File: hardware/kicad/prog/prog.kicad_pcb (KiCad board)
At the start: 2 copper layers, 174 x 134 mm, 1 part, among them J1 AES_PROG

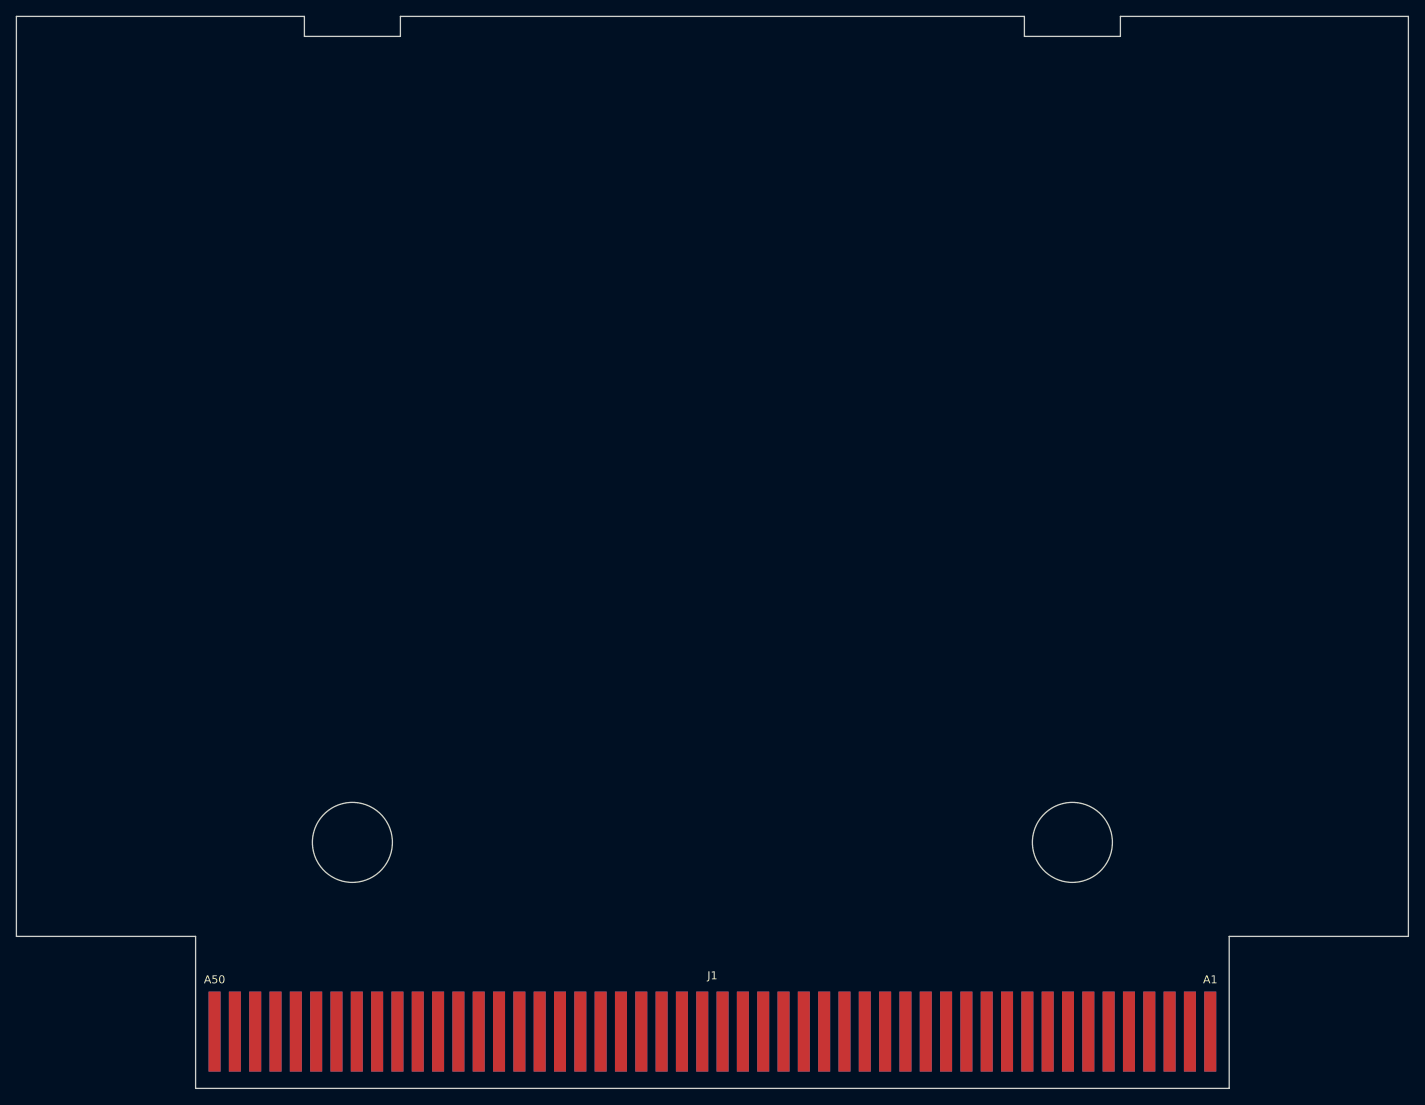
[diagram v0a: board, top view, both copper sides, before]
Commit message: Circuits imprimés 2 couches : placement et affectation des broches FPGA
- hardware/gen/pcb.py : empreintes et réseaux depuis boards.py, contour
  depuis outline.py ; ancres placées (contacts, rangée de tampons, FPGA,
  mémoires ; CHA : Pico au centre, microSD et bouton en haut), passifs
  au plus près de leur broche, masse coulée sur les deux faces.
- --pins : signaux des FPGA affectés aux broches tournées vers leur
  cible en conservant l'ordre circulaire (pins_opt.json, repris par
  fpga_pins.py) ; stable en trois passes.
- boards.py : canaux des tampons triés selon la position des contacts.
- hardware/gen/route.py : export Specctra, Freerouting, relecture de la
  session, DRC.
Placement-routage FPGA avec les nouvelles broches : en cours de
vérification.

Co-Authored-By: Claude Opus 5.5 <noreply@anthropic.com>
Claude-Session: https://claude.ai/code/session_01WKfXP1YJ8otGxZ5dsY6Agh
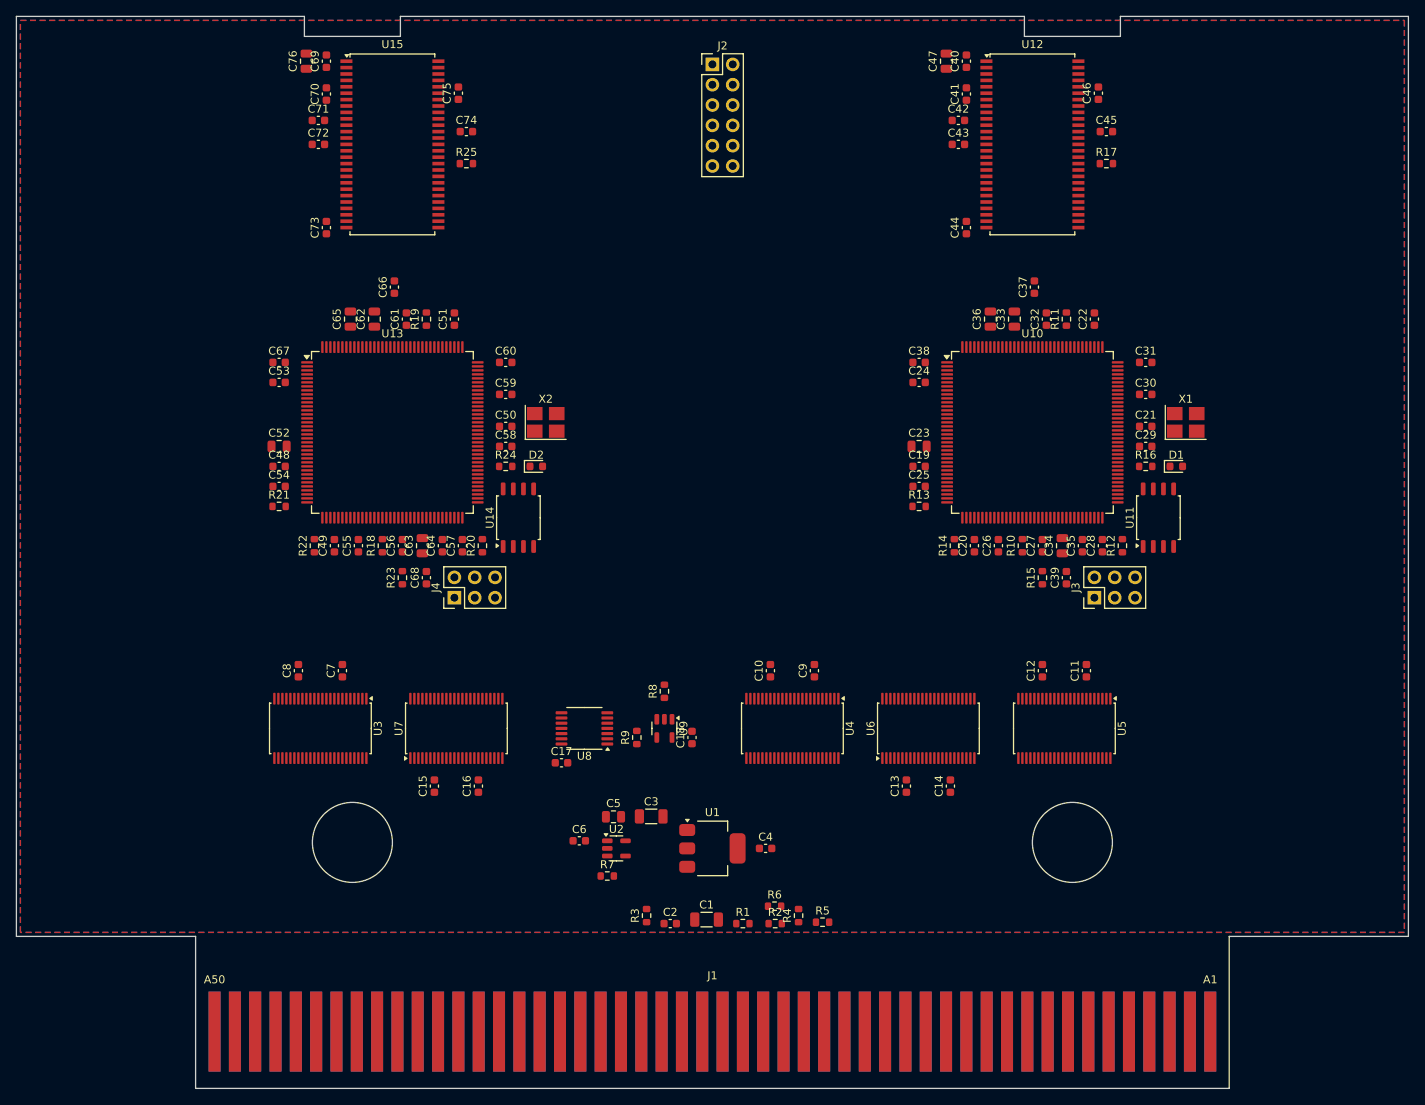
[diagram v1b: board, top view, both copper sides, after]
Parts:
- added C1: 22u, Capacitor_SMD:C_1206_3216Metric, F.Cu at (149.3, 158.9)
- added C10: 100n, Capacitor_SMD:C_0603_1608Metric, F.Cu at (157.2, 127.8)
- added C11: 100n, Capacitor_SMD:C_0603_1608Metric, F.Cu at (196.8, 127.8)
- added C12: 100n, Capacitor_SMD:C_0603_1608Metric, F.Cu at (191.2, 127.8)
- added C13: 100n, Capacitor_SMD:C_0603_1608Metric, F.Cu at (174.2, 142.2)
- added C14: 100n, Capacitor_SMD:C_0603_1608Metric, F.Cu at (179.8, 142.2)
- added C15: 100n, Capacitor_SMD:C_0603_1608Metric, F.Cu at (115.2, 142.2)
- added C16: 100n, Capacitor_SMD:C_0603_1608Metric, F.Cu at (120.8, 142.2)
- added C17: 100n, Capacitor_SMD:C_0603_1608Metric, F.Cu at (131.1, 139.3)
- added C18: 100n, Capacitor_SMD:C_0603_1608Metric, F.Cu at (147.4, 136.1)
- added C19: 100n, Capacitor_SMD:C_0603_1608Metric, F.Cu at (175.8, 102.2)
- added C2: 100n, Capacitor_SMD:C_0603_1608Metric, F.Cu at (144.7, 159.4)
- added C20: 100n, Capacitor_SMD:C_0603_1608Metric, F.Cu at (182.8, 112.2)
- added C21: 100n, Capacitor_SMD:C_0603_1608Metric, F.Cu at (204.2, 97.2)
- added C22: 100n, Capacitor_SMD:C_0603_1608Metric, F.Cu at (197.8, 83.8)
- added C23: 10u, Capacitor_SMD:C_0805_2012Metric, F.Cu at (175.8, 99.8)
- added C24: 100n, Capacitor_SMD:C_0603_1608Metric, F.Cu at (175.8, 91.8)
- added C25: 100n, Capacitor_SMD:C_0603_1608Metric, F.Cu at (175.8, 104.8)
- added C26: 100n, Capacitor_SMD:C_0603_1608Metric, F.Cu at (185.8, 112.2)
- added C27: 100n, Capacitor_SMD:C_0603_1608Metric, F.Cu at (191.2, 112.2)
- added C28: 100n, Capacitor_SMD:C_0603_1608Metric, F.Cu at (198.8, 112.2)
- added C29: 100n, Capacitor_SMD:C_0603_1608Metric, F.Cu at (204.2, 99.8)
- added C3: 22u, Capacitor_SMD:C_1206_3216Metric, F.Cu at (142.3, 146.0)
- added C30: 100n, Capacitor_SMD:C_0603_1608Metric, F.Cu at (204.2, 93.2)
- added C31: 100n, Capacitor_SMD:C_0603_1608Metric, F.Cu at (204.2, 89.2)
- added C32: 100n, Capacitor_SMD:C_0603_1608Metric, F.Cu at (191.8, 83.8)
- added C33: 10u, Capacitor_SMD:C_0805_2012Metric, F.Cu at (187.8, 83.8)
- added C34: 10u, Capacitor_SMD:C_0805_2012Metric, F.Cu at (193.8, 112.2)
- added C35: 100n, Capacitor_SMD:C_0603_1608Metric, F.Cu at (196.2, 112.2)
- added C36: 10u, Capacitor_SMD:C_0805_2012Metric, F.Cu at (184.8, 83.8)
- added C37: 100n, Capacitor_SMD:C_0603_1608Metric, F.Cu at (190.2, 79.8)
- added C38: 100n, Capacitor_SMD:C_0603_1608Metric, F.Cu at (175.8, 89.2)
- added C39: 100n, Capacitor_SMD:C_0603_1608Metric, F.Cu at (194.2, 116.2)
- added C4: 100n, Capacitor_SMD:C_0603_1608Metric, F.Cu at (156.7, 150.0)
- added C40: 100n, Capacitor_SMD:C_0603_1608Metric, F.Cu at (181.8, 51.6)
- added C41: 100n, Capacitor_SMD:C_0603_1608Metric, F.Cu at (181.8, 55.7)
- added C42: 100n, Capacitor_SMD:C_0603_1608Metric, F.Cu at (180.8, 59.0)
- added C43: 100n, Capacitor_SMD:C_0603_1608Metric, F.Cu at (180.8, 62.0)
- added C44: 100n, Capacitor_SMD:C_0603_1608Metric, F.Cu at (181.8, 72.4)
- added C45: 100n, Capacitor_SMD:C_0603_1608Metric, F.Cu at (199.2, 60.4)
- added C46: 100n, Capacitor_SMD:C_0603_1608Metric, F.Cu at (198.2, 55.6)
- added C47: 10u, Capacitor_SMD:C_0805_2012Metric, F.Cu at (179.2, 51.6)
- added C48: 100n, Capacitor_SMD:C_0603_1608Metric, F.Cu at (95.8, 102.2)
- added C49: 100n, Capacitor_SMD:C_0603_1608Metric, F.Cu at (102.8, 112.2)
- added C5: 10u, Capacitor_SMD:C_0805_2012Metric, F.Cu at (137.6, 146.1)
- added C50: 100n, Capacitor_SMD:C_0603_1608Metric, F.Cu at (124.2, 97.2)
- added C51: 100n, Capacitor_SMD:C_0603_1608Metric, F.Cu at (117.8, 83.8)
- added C52: 10u, Capacitor_SMD:C_0805_2012Metric, F.Cu at (95.8, 99.8)
- added C53: 100n, Capacitor_SMD:C_0603_1608Metric, F.Cu at (95.8, 91.8)
- added C54: 100n, Capacitor_SMD:C_0603_1608Metric, F.Cu at (95.8, 104.8)
- added C55: 100n, Capacitor_SMD:C_0603_1608Metric, F.Cu at (105.8, 112.2)
- added C56: 100n, Capacitor_SMD:C_0603_1608Metric, F.Cu at (111.2, 112.2)
- added C57: 100n, Capacitor_SMD:C_0603_1608Metric, F.Cu at (118.8, 112.2)
- added C58: 100n, Capacitor_SMD:C_0603_1608Metric, F.Cu at (124.2, 99.8)
- added C59: 100n, Capacitor_SMD:C_0603_1608Metric, F.Cu at (124.2, 93.2)
- added C6: 1u, Capacitor_SMD:C_0603_1608Metric, F.Cu at (133.4, 149.1)
- added C60: 100n, Capacitor_SMD:C_0603_1608Metric, F.Cu at (124.2, 89.2)
- added C61: 100n, Capacitor_SMD:C_0603_1608Metric, F.Cu at (111.8, 83.8)
- added C62: 10u, Capacitor_SMD:C_0805_2012Metric, F.Cu at (107.8, 83.8)
- added C63: 10u, Capacitor_SMD:C_0805_2012Metric, F.Cu at (113.8, 112.2)
- added C64: 100n, Capacitor_SMD:C_0603_1608Metric, F.Cu at (116.2, 112.2)
- added C65: 10u, Capacitor_SMD:C_0805_2012Metric, F.Cu at (104.8, 83.8)
- added C66: 100n, Capacitor_SMD:C_0603_1608Metric, F.Cu at (110.2, 79.8)
- added C67: 100n, Capacitor_SMD:C_0603_1608Metric, F.Cu at (95.8, 89.2)
- added C68: 100n, Capacitor_SMD:C_0603_1608Metric, F.Cu at (114.2, 116.2)
- added C69: 100n, Capacitor_SMD:C_0603_1608Metric, F.Cu at (101.8, 51.6)
- added C7: 100n, Capacitor_SMD:C_0603_1608Metric, F.Cu at (103.8, 127.8)
- added C70: 100n, Capacitor_SMD:C_0603_1608Metric, F.Cu at (101.8, 55.7)
- added C71: 100n, Capacitor_SMD:C_0603_1608Metric, F.Cu at (100.8, 59.0)
- added C72: 100n, Capacitor_SMD:C_0603_1608Metric, F.Cu at (100.8, 62.0)
- added C73: 100n, Capacitor_SMD:C_0603_1608Metric, F.Cu at (101.8, 72.4)
- added C74: 100n, Capacitor_SMD:C_0603_1608Metric, F.Cu at (119.2, 60.4)
- added C75: 100n, Capacitor_SMD:C_0603_1608Metric, F.Cu at (118.2, 55.6)
- added C76: 10u, Capacitor_SMD:C_0805_2012Metric, F.Cu at (99.2, 51.6)
- added C8: 100n, Capacitor_SMD:C_0603_1608Metric, F.Cu at (98.2, 127.8)
- added C9: 100n, Capacitor_SMD:C_0603_1608Metric, F.Cu at (162.8, 127.8)
- added D1: LED, LED_SMD:LED_0603_1608Metric, F.Cu at (208.0, 102.2)
- added D2: LED, LED_SMD:LED_0603_1608Metric, F.Cu at (128.0, 102.2)
- added J2: Câble PROG-CHA, Connector_PinHeader_2.54mm:PinHeader_2x06_P2.54mm_Vertical, F.Cu at (150.0, 52.0)
- added J3: PROG P, Connector_PinHeader_2.54mm:PinHeader_2x03_P2.54mm_Vertical, F.Cu at (197.8, 118.7)
- added J4: PROG V, Connector_PinHeader_2.54mm:PinHeader_2x03_P2.54mm_Vertical, F.Cu at (117.8, 118.7)
- added R1: 0, Resistor_SMD:R_0603_1608Metric, F.Cu at (153.8, 159.4)
- added R10: 100, Resistor_SMD:R_0603_1608Metric, F.Cu at (188.8, 112.2)
- added R11: 100, Resistor_SMD:R_0603_1608Metric, F.Cu at (194.2, 83.8)
- added R12: 10k, Resistor_SMD:R_0603_1608Metric, F.Cu at (201.2, 112.2)
- added R13: 10k, Resistor_SMD:R_0603_1608Metric, F.Cu at (175.8, 107.2)
- added R14: 10k, Resistor_SMD:R_0603_1608Metric, F.Cu at (180.2, 112.2)
- added R15: 10k, Resistor_SMD:R_0603_1608Metric, F.Cu at (191.2, 116.2)
- added R16: 470, Resistor_SMD:R_0603_1608Metric, F.Cu at (204.2, 102.2)
- added R17: 33, Resistor_SMD:R_0603_1608Metric, F.Cu at (199.2, 64.4)
- added R18: 100, Resistor_SMD:R_0603_1608Metric, F.Cu at (108.8, 112.2)
- added R19: 100, Resistor_SMD:R_0603_1608Metric, F.Cu at (114.2, 83.8)
- added R2: 0, Resistor_SMD:R_0603_1608Metric, F.Cu at (157.8, 159.4)
- added R20: 10k, Resistor_SMD:R_0603_1608Metric, F.Cu at (121.2, 112.2)
- added R21: 10k, Resistor_SMD:R_0603_1608Metric, F.Cu at (95.8, 107.2)
- added R22: 10k, Resistor_SMD:R_0603_1608Metric, F.Cu at (100.2, 112.2)
- added R23: 10k, Resistor_SMD:R_0603_1608Metric, F.Cu at (111.2, 116.2)
- added R24: 470, Resistor_SMD:R_0603_1608Metric, F.Cu at (124.2, 102.2)
- added R25: 33, Resistor_SMD:R_0603_1608Metric, F.Cu at (119.2, 64.4)
- added R3: 10k, Resistor_SMD:R_0603_1608Metric, F.Cu at (141.8, 158.4)
- added R4: 10k, Resistor_SMD:R_0603_1608Metric, F.Cu at (160.8, 158.4)
- added R5: 10k, Resistor_SMD:R_0603_1608Metric, F.Cu at (163.8, 159.2)
- added R6: 10k, Resistor_SMD:R_0603_1608Metric, F.Cu at (157.8, 157.2)
- added R7: 10k, Resistor_SMD:R_0603_1608Metric, F.Cu at (136.9, 153.4)
- added R8: 10k, Resistor_SMD:R_0603_1608Metric, F.Cu at (144.0, 130.4)
- added R9: 10k, Resistor_SMD:R_0603_1608Metric, F.Cu at (140.6, 136.1)
- added U1: AMS1117-3.3, Package_TO_SOT_SMD:SOT-223-3_TabPin2, F.Cu at (150.0, 150.0)
- added U10: iCE40HX4K-TQ144, Package_QFP:TQFP-144_20x20mm_P0.5mm, F.Cu at (190.0, 98.0)
- added U11: W25Q32JVSS, Package_SO:SOIC-8_5.23x5.23mm_P1.27mm, F.Cu at (205.8, 108.7)
- added U12: W9825G6KH-6, Package_SO:TSOP-II-54_22.2x10.16mm_P0.8mm, F.Cu at (190.0, 62.0)
- added U13: iCE40HX4K-TQ144, Package_QFP:TQFP-144_20x20mm_P0.5mm, F.Cu at (110.0, 98.0)
- added U14: W25Q32JVSS, Package_SO:SOIC-8_5.23x5.23mm_P1.27mm, F.Cu at (125.8, 108.7)
- added U15: W9825G6KH-6, Package_SO:TSOP-II-54_22.2x10.16mm_P0.8mm, F.Cu at (110.0, 62.0)
- added U2: AP2112K-1.2, Package_TO_SOT_SMD:SOT-23-5, F.Cu at (138.0, 150.0)
- added U3: 74LVC16244A, Package_SO:TSSOP-48_6.1x12.5mm_P0.5mm, F.Cu at (101.0, 135.0)
- added U4: 74LVC16244A, Package_SO:TSSOP-48_6.1x12.5mm_P0.5mm, F.Cu at (160.0, 135.0)
- added U5: 74LVC16244A, Package_SO:TSSOP-48_6.1x12.5mm_P0.5mm, F.Cu at (194.0, 135.0)
- added U6: 74LVC16245A, Package_SO:TSSOP-48_6.1x12.5mm_P0.5mm, F.Cu at (177.0, 135.0)
- added U7: 74LVC16245A, Package_SO:TSSOP-48_6.1x12.5mm_P0.5mm, F.Cu at (118.0, 135.0)
- added U8: 74AHCT125, Package_SO:TSSOP-14_4.4x5mm_P0.65mm, F.Cu at (134.0, 135.0)
- added U9: 74LVC1G07, Package_TO_SOT_SMD:SOT-23-5, F.Cu at (144.0, 135.0)
- added X1: 25 MHz 3,3 V, Oscillator:Oscillator_SMD_Abracon_ASE-4Pin_3.2x2.5mm_HandSoldering, F.Cu at (209.2, 96.8)
- added X2: 25 MHz 3,3 V, Oscillator:Oscillator_SMD_Abracon_ASE-4Pin_3.2x2.5mm_HandSoldering, F.Cu at (129.2, 96.8)
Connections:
- J1 pad B1: (no net) -> GND
- J1 pad B10: (no net) -> AES_A8
- J1 pad B11: (no net) -> AES_A9
- J1 pad B12: (no net) -> AES_A10
- J1 pad B13: (no net) -> AES_A11
- J1 pad B14: (no net) -> AES_A12
- J1 pad B15: (no net) -> AES_A13
- J1 pad B16: (no net) -> AES_A14
- J1 pad B17: (no net) -> AES_A15
- J1 pad B18: (no net) -> AES_A16
- J1 pad B19: (no net) -> AES_A17
- J1 pad B2: (no net) -> GND
- J1 pad B20: (no net) -> AES_A18
- J1 pad B21: (no net) -> AES_A19
- J1 pad B22: (no net) -> AES_ROMOE
- J1 pad B23: (no net) -> AES_R_OUT
- J1 pad B24: (no net) -> AES_R_IN
- J1 pad B25: (no net) -> +5V
- J1 pad B26: (no net) -> +5V
- J1 pad B27: (no net) -> +5V
- J1 pad B28: (no net) -> AES_ROMWAIT
- J1 pad B29: (no net) -> AES_PDTACK
- J1 pad B3: (no net) -> AES_A1
- J1 pad B30: (no net) -> AES_PWAIT0
- J1 pad B31: (no net) -> AES_PWAIT1
- J1 pad B32: (no net) -> AES_SDRAD0
- J1 pad B33: (no net) -> AES_SDRAD1
- J1 pad B34: (no net) -> AES_SDRAD2
- J1 pad B35: (no net) -> AES_SDRAD3
- J1 pad B36: (no net) -> AES_SDRAD4
- J1 pad B37: (no net) -> AES_SDRAD5
- J1 pad B38: (no net) -> AES_SDRAD6
- J1 pad B39: (no net) -> AES_SDRAD7
- J1 pad B4: (no net) -> AES_A2
- J1 pad B40: (no net) -> AES_SDRA8
- J1 pad B41: (no net) -> AES_SDRA9
- J1 pad B42: (no net) -> AES_SDRA20
- J1 pad B43: (no net) -> AES_SDRA21
- J1 pad B44: (no net) -> AES_SDRA22
- J1 pad B45: (no net) -> AES_SDRA23
- J1 pad B46: (no net) -> AES_SDRMPX
- J1 pad B47: (no net) -> AES_SDROE
- J1 pad B49: (no net) -> GND
- J1 pad B5: (no net) -> AES_A3
- J1 pad B50: (no net) -> GND
- J1 pad B6: (no net) -> AES_A4
- J1 pad B7: (no net) -> AES_A5
- J1 pad B8: (no net) -> AES_A6
- J1 pad B9: (no net) -> AES_A7
- J1 pad T1: (no net) -> GND
- J1 pad T10: (no net) -> AES_D7
- J1 pad T11: (no net) -> AES_D8
- J1 pad T12: (no net) -> AES_D9
- J1 pad T13: (no net) -> AES_D10
- J1 pad T14: (no net) -> AES_D11
- J1 pad T15: (no net) -> AES_D12
- J1 pad T16: (no net) -> AES_D13
- J1 pad T17: (no net) -> AES_D14
- J1 pad T18: (no net) -> AES_D15
- J1 pad T2: (no net) -> GND
- J1 pad T23: (no net) -> AES_L_OUT
- J1 pad T24: (no net) -> AES_L_IN
- J1 pad T25: (no net) -> +5V
- J1 pad T26: (no net) -> +5V
- J1 pad T27: (no net) -> +5V
- J1 pad T28: (no net) -> AES_PORTOEU
- J1 pad T29: (no net) -> AES_PORTOEL
- J1 pad T3: (no net) -> AES_D0
- J1 pad T30: (no net) -> AES_PORTWEU
- J1 pad T31: (no net) -> AES_PORTWEL
- J1 pad T34: (no net) -> AES_SDPAD0
- J1 pad T35: (no net) -> AES_SDPAD1
- J1 pad T36: (no net) -> AES_SDPAD2
- J1 pad T37: (no net) -> AES_SDPAD3
- J1 pad T38: (no net) -> AES_SDPAD4
- J1 pad T39: (no net) -> AES_SDPAD5
- J1 pad T4: (no net) -> AES_D1
- J1 pad T40: (no net) -> AES_SDPAD6
- J1 pad T41: (no net) -> AES_SDPAD7
- J1 pad T42: (no net) -> AES_SDPA8
- J1 pad T43: (no net) -> AES_SDPA9
- J1 pad T44: (no net) -> AES_SDPA10
- J1 pad T45: (no net) -> AES_SDPA11
- J1 pad T46: (no net) -> AES_SDPMPX
- J1 pad T47: (no net) -> AES_SDPOE
- J1 pad T49: (no net) -> GND
- J1 pad T5: (no net) -> AES_D2
- J1 pad T50: (no net) -> GND
- J1 pad T6: (no net) -> AES_D3
- J1 pad T7: (no net) -> AES_D4
- J1 pad T8: (no net) -> AES_D5
- J1 pad T9: (no net) -> AES_D6
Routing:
- added copper zone on B.Cu, net GND
- added copper zone on F.Cu, net GND

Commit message: Circuits imprimés en 4 couches
Empilement F.Cu signaux / In1 masse / In2 +3V3 / B.Cu signaux : chemin
de retour continu pour la SDRAM à 100 MHz et découplage des FPGA.
route.py déclare les couches internes « power » pour Freerouting.
Doc : fréquences des FPGA avec les broches du circuit imprimé (P à
100,2 MHz, limite).

Co-Authored-By: Claude Opus 5.5 <noreply@anthropic.com>
Claude-Session: https://claude.ai/code/session_01WKfXP1YJ8otGxZ5dsY6Agh
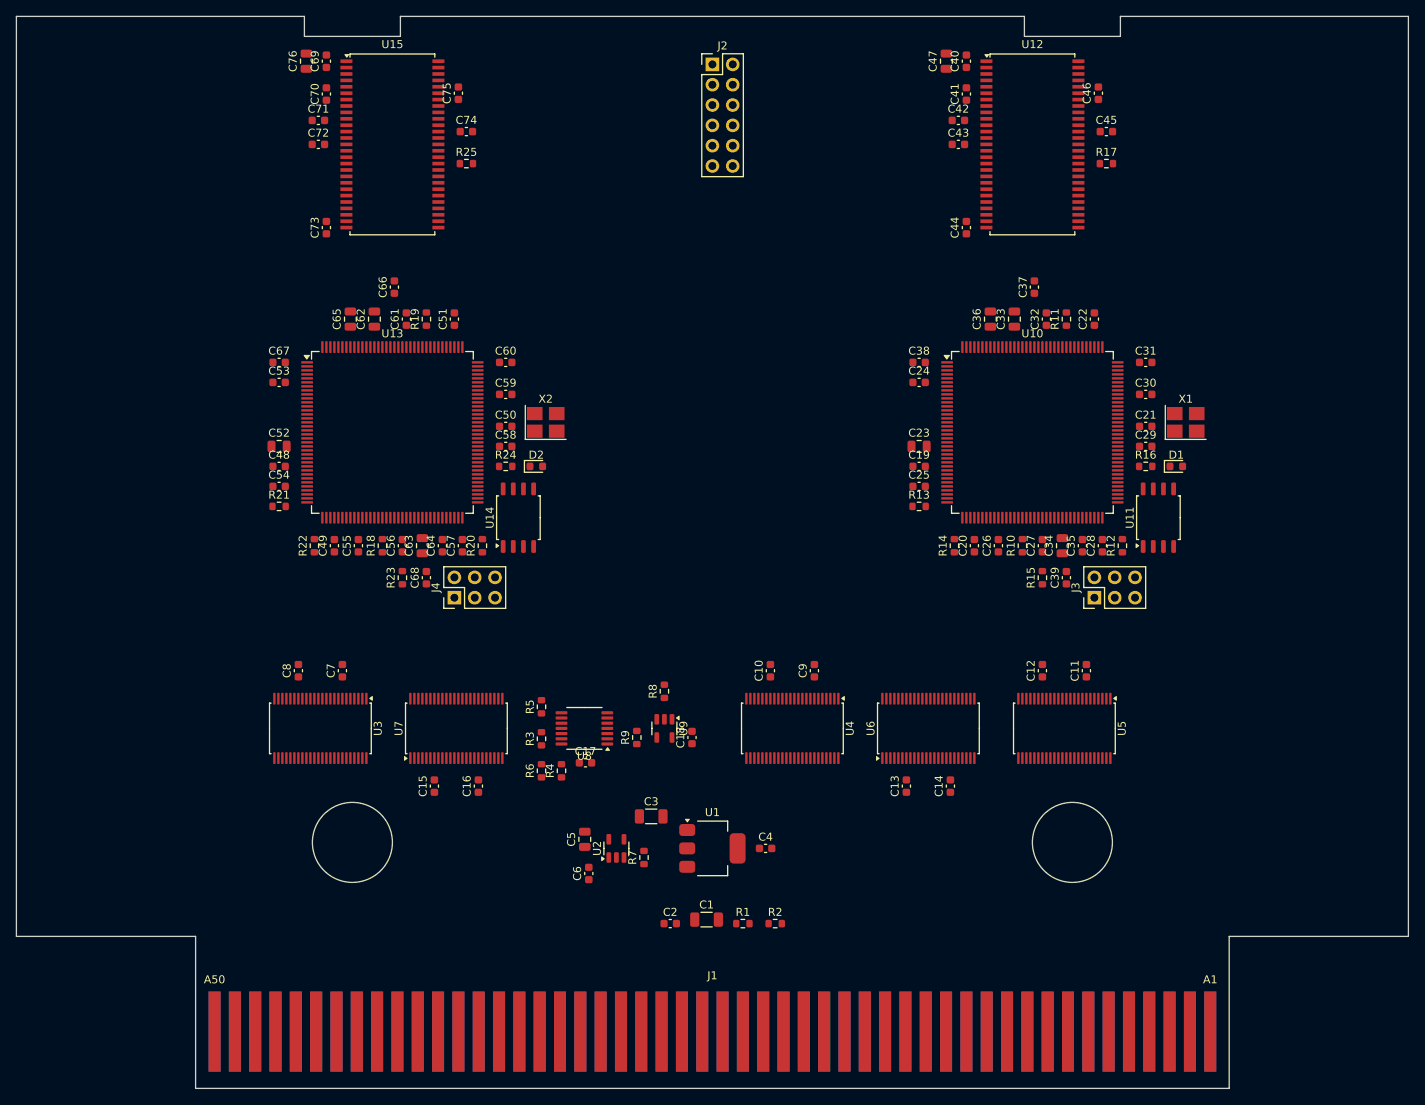
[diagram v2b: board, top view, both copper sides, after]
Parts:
- moved R5 44.3 mm to (128.6, 132.3), turned to 90 degrees
- moved R4 34.7 mm to (131.1, 140.3)
- moved R6 33.7 mm to (128.6, 140.3), turned to 90 degrees
- moved R3 25.7 mm to (128.6, 136.3)
- moved R7 5.14 mm to (141.4, 151.1), turned to 90 degrees
- moved C5 4.56 mm to (134.1, 148.9), turned to 90 degrees
- moved C6 4.26 mm to (134.6, 153.1), turned to 90 degrees
- moved C17 3.00 mm to (134.1, 139.3)
- turned U2 to 90 degrees
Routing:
- added copper zone on In2.Cu, net +3V3
- added copper zone on In1.Cu, net GND
- removed copper zone on B.Cu, net GND
- removed copper zone on F.Cu, net GND
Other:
- copper layers 2 -> 4

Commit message: PCB : découplage sous les boîtiers, en face arrière
Les condensateurs de découplage des FPGA, mémoires et tampons, placés
devant les rangées de broches, bloquaient leur sortie (premier essai
de routage : 52 % des broches sorties, 116 liaisons non routées). Ils
sont désormais sous le boîtier, face arrière, reliés aux plans par
des vias courts.

Co-Authored-By: Claude Opus 5.5 <noreply@anthropic.com>
Claude-Session: https://claude.ai/code/session_01WKfXP1YJ8otGxZ5dsY6Agh
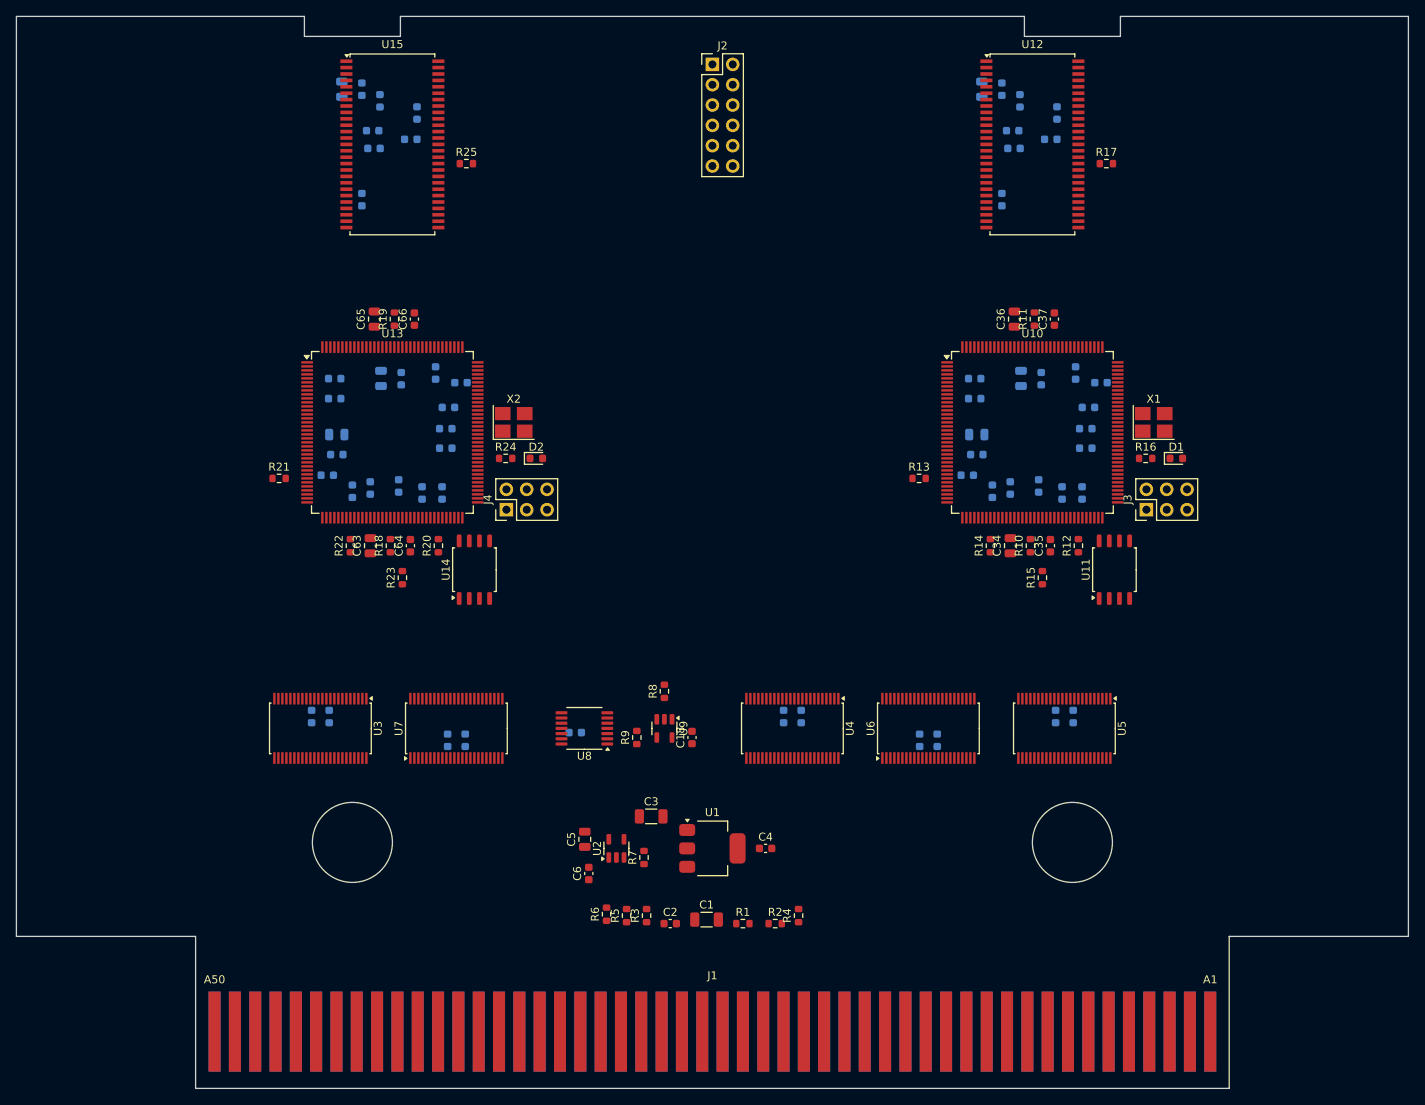
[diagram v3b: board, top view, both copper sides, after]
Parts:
- C10, C11, C12, C13, C14, C15, C16, C17, C19, C20, C21, C22, C23, C24, C25, C26, C27, C28, C29, C30, C31, C32, C33, C38, C39, C40, C41, C42, C43, C44, C45, C46, C47, C48, C49, C50, C51, C52, C53, C54, C55, C56, C57, C58, C59, C60, C61, C62, C67, C68, C69, C7, C70, C71, C72, C73, C74, C75, C76, C8, C9: moved to B.Cu
- moved R4 34.7 mm to (160.8, 158.4)
- moved R5 28.2 mm to (139.3, 158.4)
- moved R3 25.7 mm to (141.8, 158.4)
- moved R6 19.7 mm to (136.8, 158.2)
- moved J3 12.8 mm to (204.2, 107.7)
- moved J4 12.8 mm to (124.2, 107.7)
- moved C39 10.6 mm to (193.7, 105.6), turned to -90 degrees
- moved C68 10.6 mm to (113.7, 105.6), turned to -90 degrees
- moved U11 8.51 mm to (200.2, 115.2)
- moved U14 8.51 mm to (120.2, 115.2)
- moved C21 7.50 mm to (196.7, 97.5)
- moved C50 7.50 mm to (116.7, 97.5)
- moved C29 7.49 mm to (196.7, 100.0)
- moved C58 7.49 mm to (116.7, 100.0)
- moved C27 7.49 mm to (190.8, 104.7), turned to -90 degrees
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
